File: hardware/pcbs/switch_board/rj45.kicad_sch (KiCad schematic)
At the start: 8 parts, among them J5 8P8C_LED

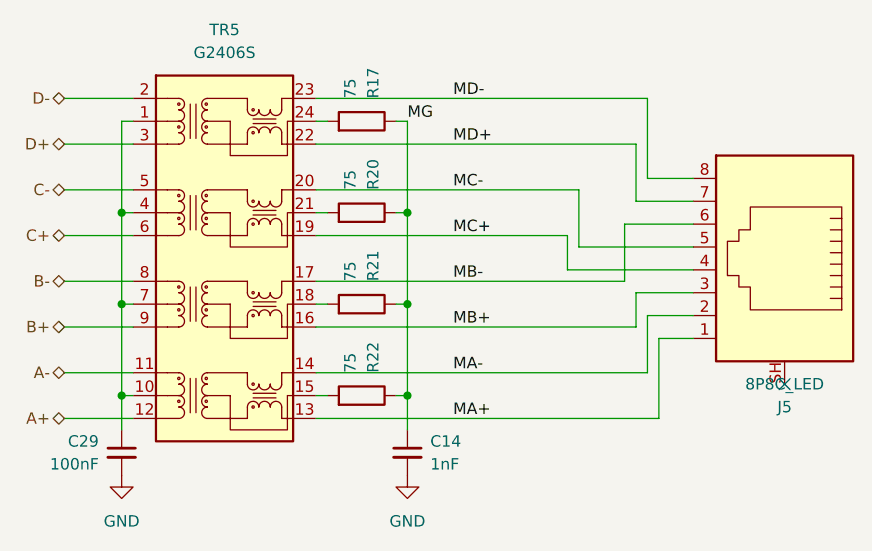
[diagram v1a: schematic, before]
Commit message: pcbs: update purchase info
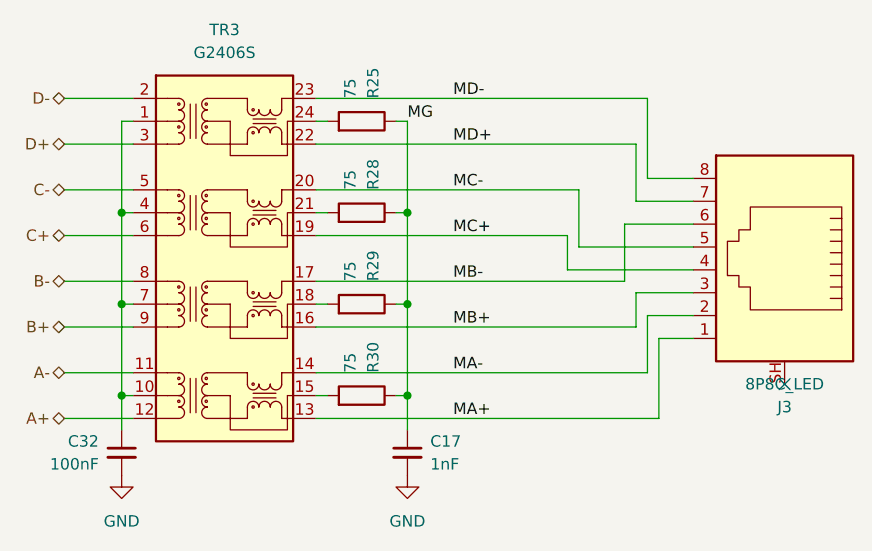
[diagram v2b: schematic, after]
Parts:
- C17: renamed from C14; Part (none) -> C 1nF 16V 0603; Shop (none) -> https://store.comet.bg/Catalogue/Product/6036/
- C32: renamed from C29; Part (none) -> C 100nF 16V 0603; Shop (none) -> https://store.comet.bg/Catalogue/Product/38000/
- J3: renamed from J5; Part (none) -> MJ88-B211-JRS3; Shop (none) -> https://www.lcsc.com/product-detail/Ethernet-Connectors-Mod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
- R25: renamed from R17; Part (none) -> R 75Ω 125mW 1% 0603; Shop (none) -> https://store.comet.bg/Catalogue/Product/35534/
- R28: renamed from R20; Part (none) -> R 75Ω 125mW 1% 0603; Shop (none) -> https://store.comet.bg/Catalogue/Product/35534/
- R29: renamed from R21; Part (none) -> R 75Ω 125mW 1% 0603; Shop (none) -> https://store.comet.bg/Catalogue/Product/35534/
- R30: renamed from R22; Part (none) -> R 75Ω 125mW 1% 0603; Shop (none) -> https://store.comet.bg/Catalogue/Product/35534/
- TR3: renamed from TR5; Part (none) -> G2406S; Shop (none) -> https://www.lcsc.com/product-detail/RJ45-Transformer_CND-te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
